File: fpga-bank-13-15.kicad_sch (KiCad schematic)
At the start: 3 parts, among them U4 XC7K160T-FFG676

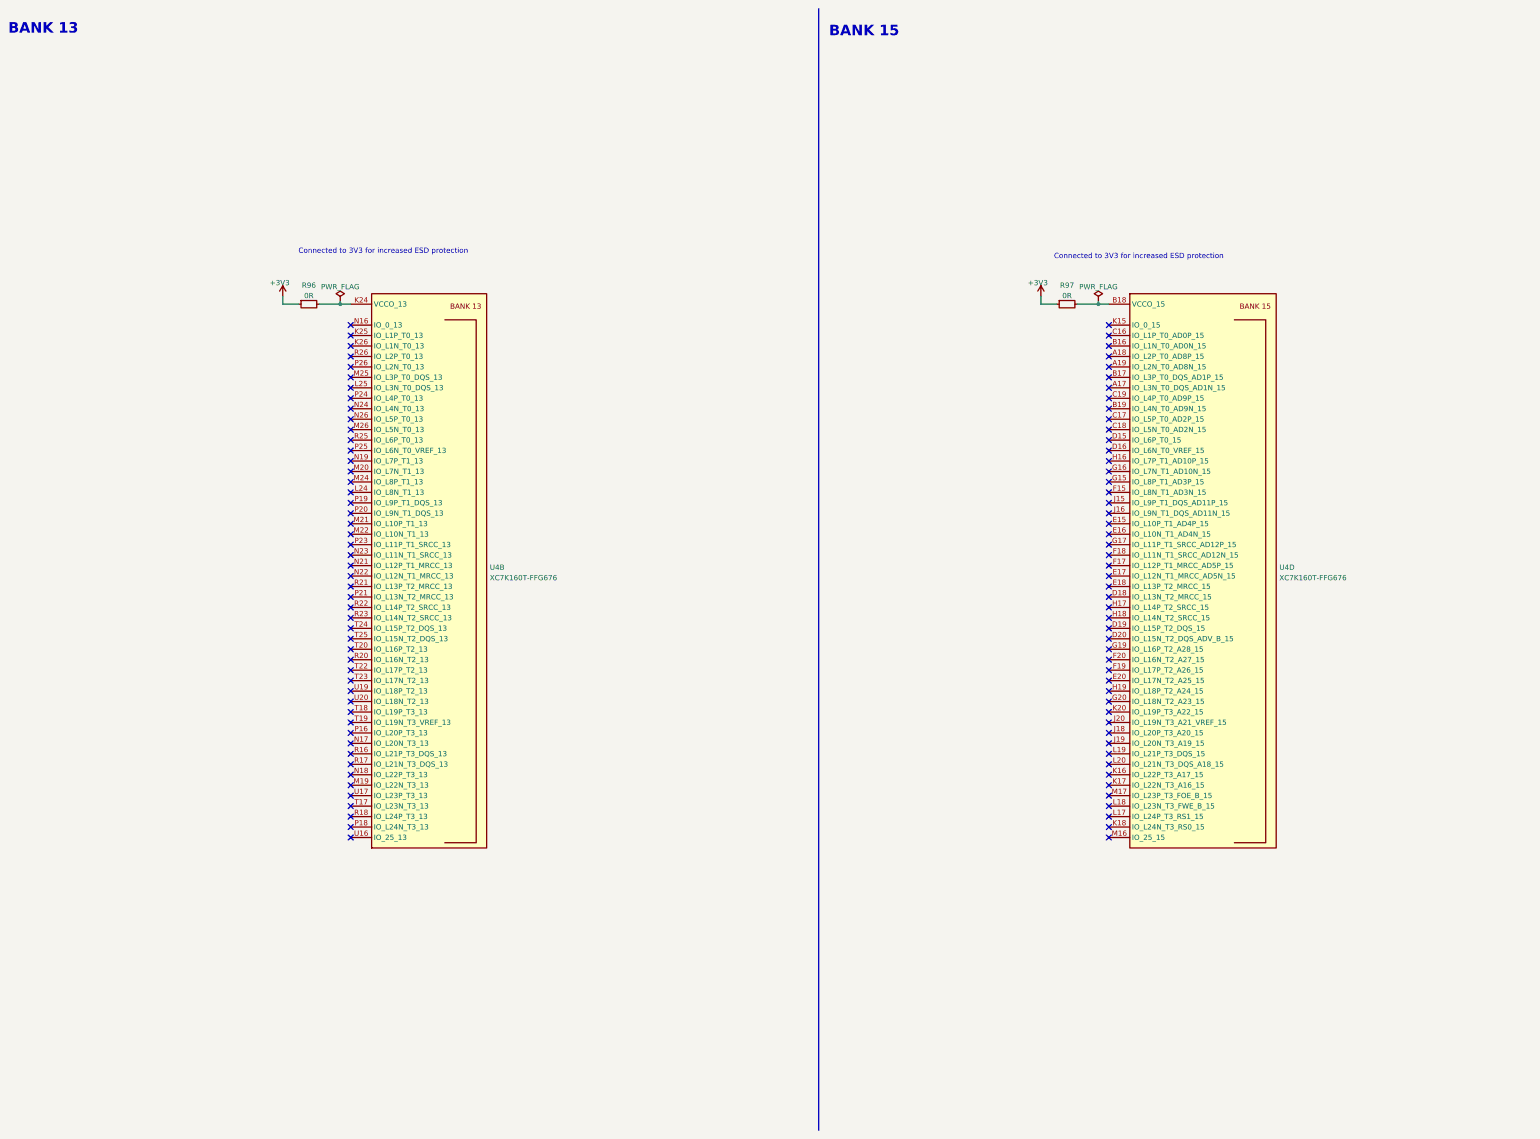
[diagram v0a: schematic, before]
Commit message: Removing PCIe from sch and PCB
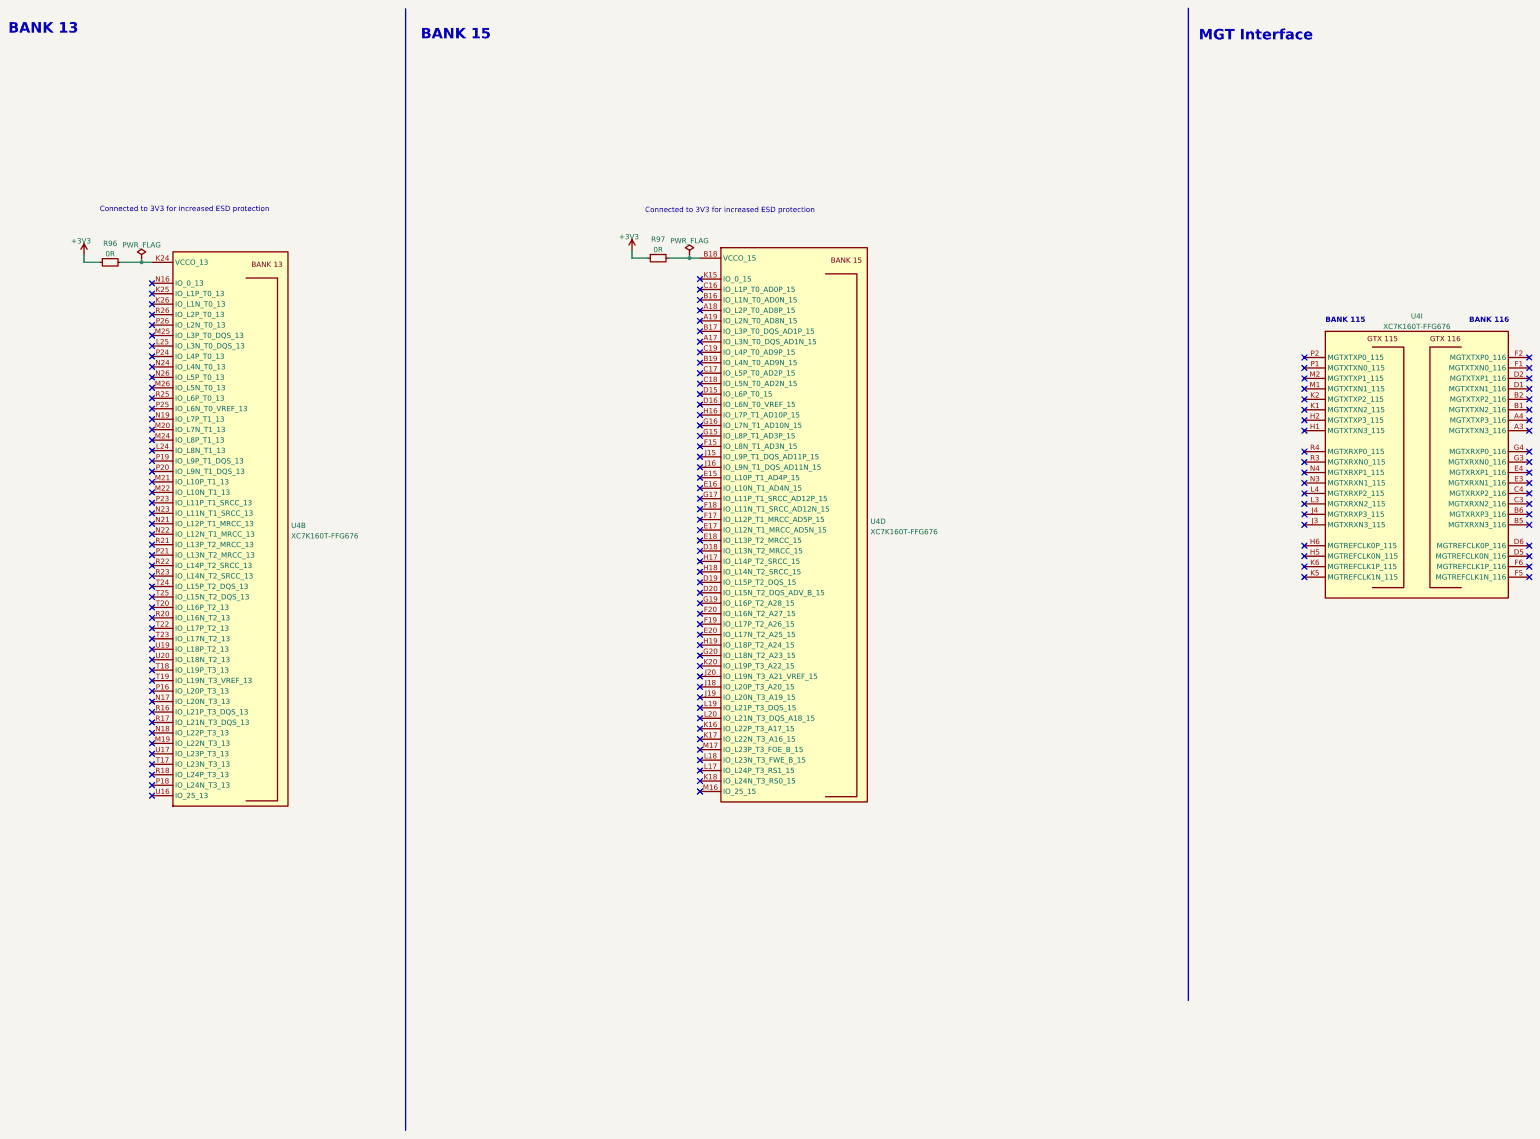
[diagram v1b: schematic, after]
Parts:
- added unit 9 of U4
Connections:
- no-connect marks 100 -> 140
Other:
- note added: "BANK 115"
- note added: "BANK 116"
- note added: "MGT Interface"
- moved on the sheet: R96, R97, U4B, U4D
